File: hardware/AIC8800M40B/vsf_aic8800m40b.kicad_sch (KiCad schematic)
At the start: 86 parts, among them J1 USB_A, J2 USB_C_Receptacle_USB2.0, J3 USB_C_Receptacle_USB2.0, J4 Micro_SD_Card_Det1, J6 Conn_Coaxial, J7 Conn_Coaxial, Q1 S9013, SW1 SW_Push, SW2 SW_Push, SW3 SW_Push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

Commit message: [hardware/aic8800m40b] update
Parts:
- removed D2: 1N5819, vllogic:D_SOD-323_BAT60, symbol Device:D_Schottky
- added C8: 22pF, Capacitor_SMD:C_0805_2012Metric, symbol Device:C
- C16: value 1pF -> 2pF
- C17, C20: value NC -> 0.5pF
- C18: value 0.5pF -> NC
- C22: value NC -> 1.5pF
- J4: footprint (none) -> VSF:MicroSD_Tiny
- J6, J7: footprint (none) -> Connector_Coaxial:U.FL_Molex_MCRF_73412-0110_Vertical
- L3: value 1.2nH -> 1.4nH
- R1: value 1.5nH -> 2nH
- R10: value 80.6k,1% -> 22K,1%
- R14: value 422k,1% -> 100K,1%
- R3: value 1.5nH -> 2pF
- R4: value 1.5nH -> 1.1nH
- U5, U6: footprint (none) -> Filter:Filter_Mini-Circuits_FV1206-1
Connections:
- net LCD_BACKLIGHT is gone; now on net GPIOB4: R13.1
- net USB_D+ is gone; now on net USB_DP: J1.3 (D+), R9.1
- net USB_D- is gone; now on net USB_DM: J1.2 (D-), R8.1
- net GPIOB2: now also J4.9 (DET)
- net PWR_3V3: now also C8.1, L4.2, C8.2
- net at C22.2, R4.1: now also U6.1 (TR_2); no longer U5.1 (TR_2)
- net at R10.2, R14.1, U4.5 (FB): now also C8.1
- net at J7.1 (In): now also U5.5 (RFIN); no longer U6.6 (RFIN)
- net at J6.1 (In): now also U6.5 (RFIN); no longer U5.6 (RFIN)
- net at C18.2, R2.2: now also U5.3 (TR_5); no longer U6.3 (TR_5)
- net at C20.1, R3.1: now also U6.3 (TR_5); no longer U5.3 (TR_5)
- net at C16.1, R1.2: now also U5.1 (TR_2); no longer U6.1 (TR_2)
- net D+: no longer names the net of J2.A6 (D+), J2.B6 (D+), R9.2
- net D-: no longer names the net of J2.A7 (D-), J2.B7 (D-), R8.2
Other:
- moved on the sheet: J5, Q1, R13

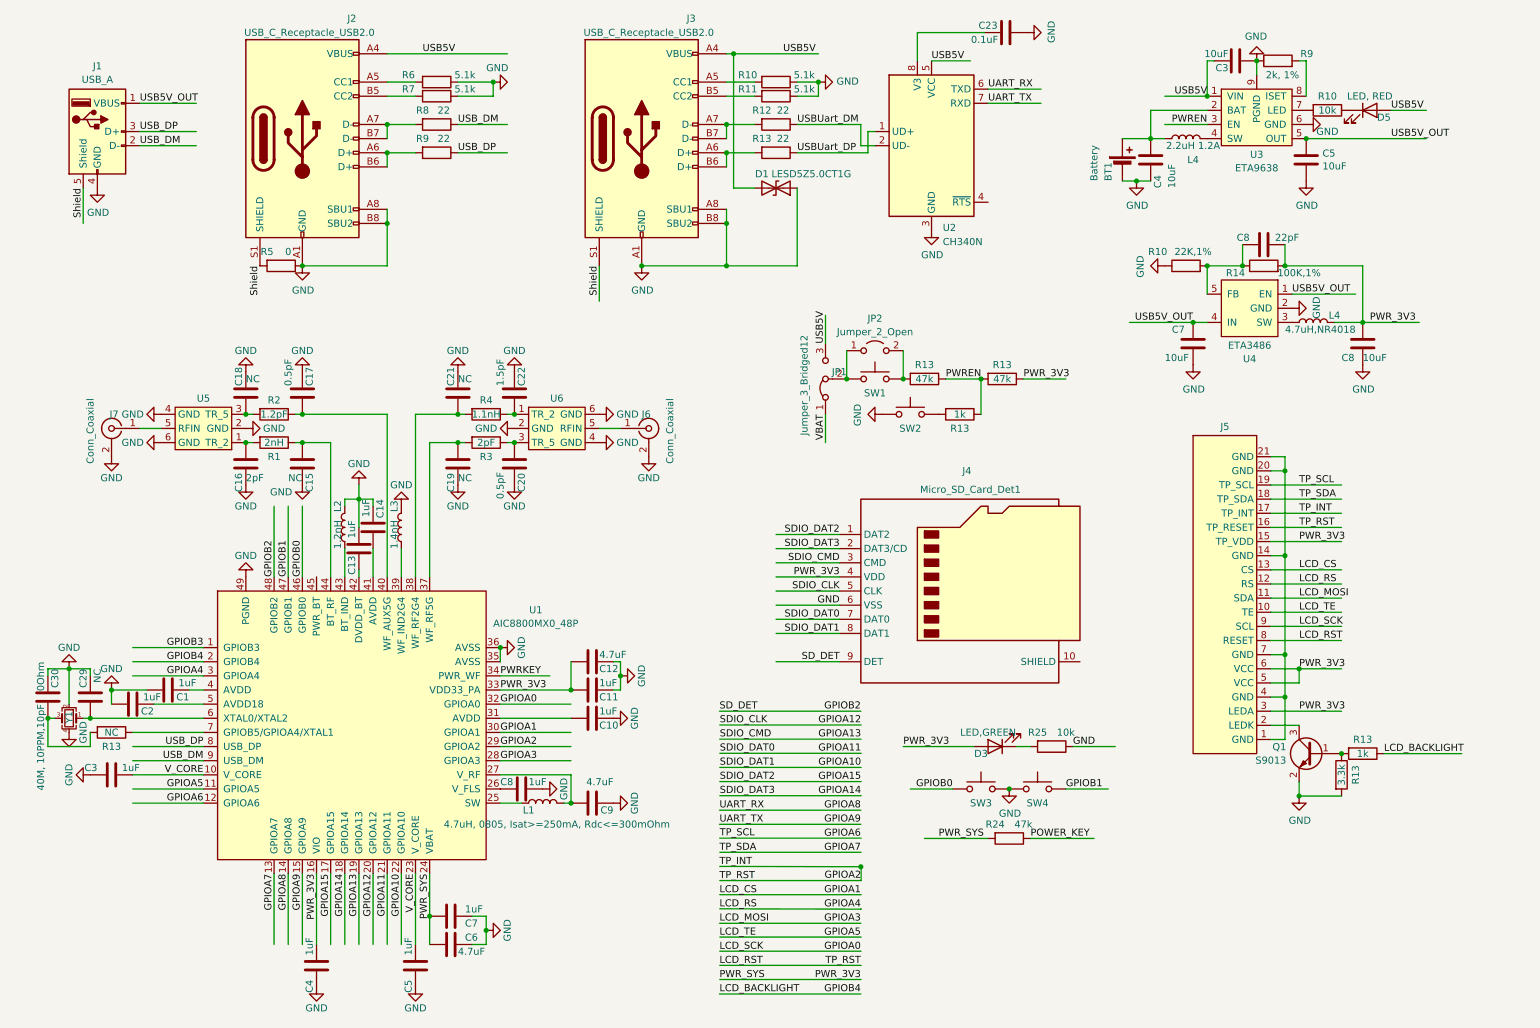
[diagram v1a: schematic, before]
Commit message: [hardware/auc8800m40b] prepare layout
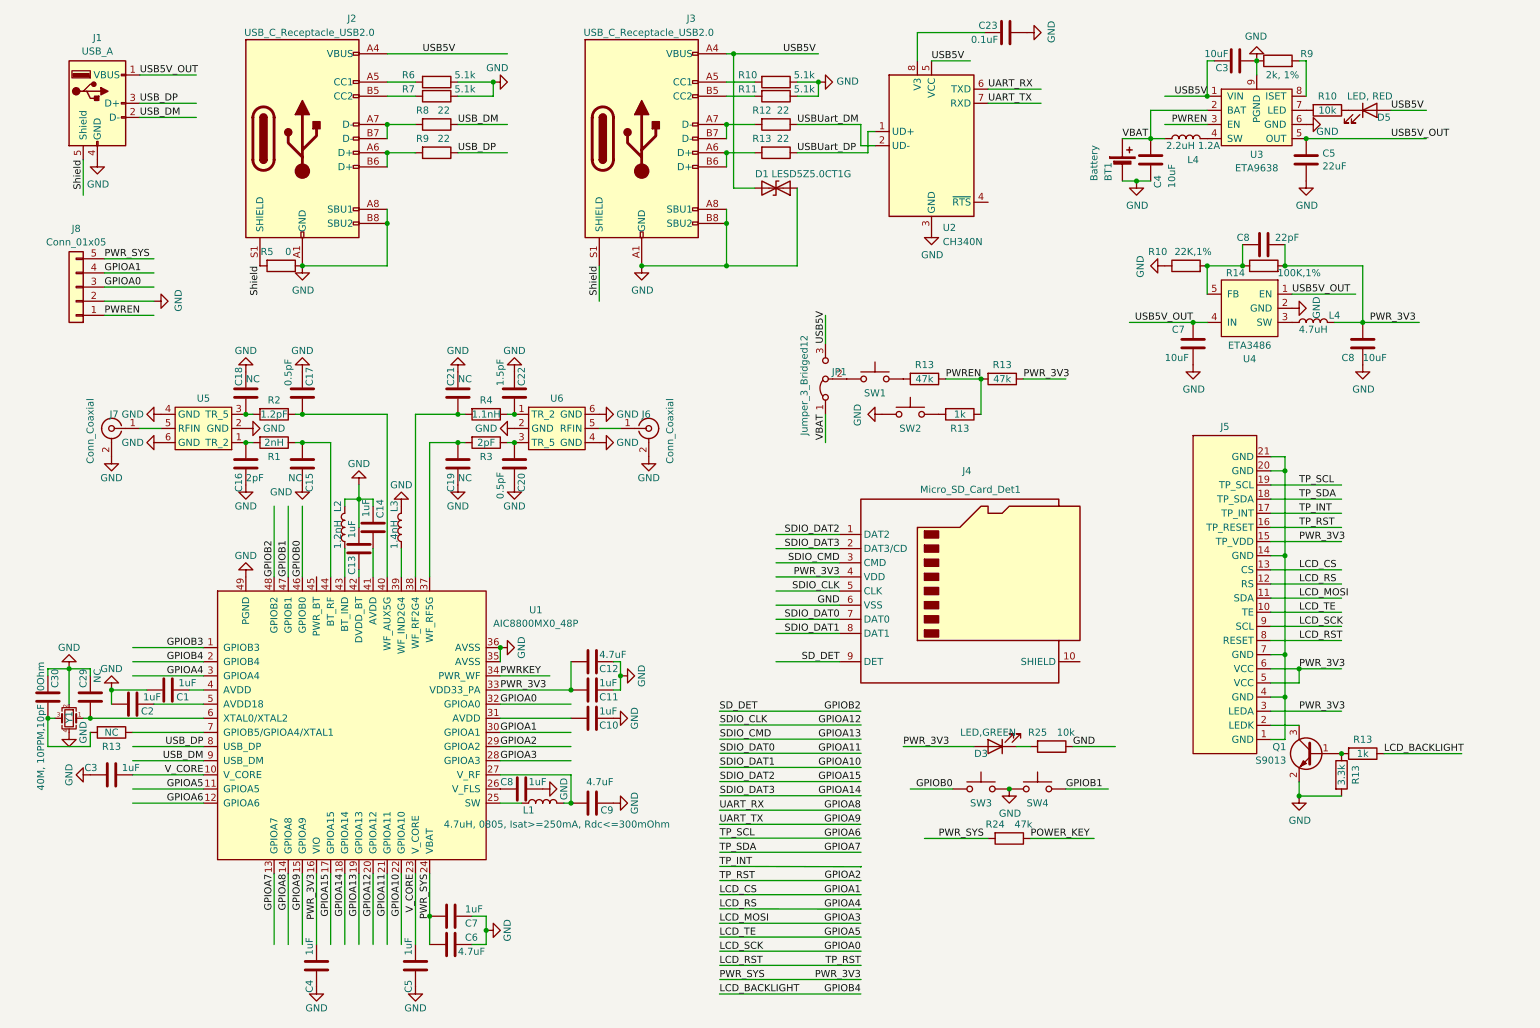
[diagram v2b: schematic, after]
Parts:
- removed JP2: Jumper_2_Open, Jumper:SolderJumper-2_P1.3mm_Open_RoundedPad1.0x1.5mm, symbol Jumper:Jumper_2_Open
- added J8: Conn_01x05, Connector_Harwin:Harwin_M20-89005xx_1x05_P2.54mm_Horizontal, symbol Connector_Generic:Conn_01x05
- C5: value 10uF -> 22uF
- C8: footprint Capacitor_SMD:C_0805_2012Metric -> Capacitor_SMD:C_0402_1005Metric
- L4: value 4.7uH,NR4018 -> 4.7uH; footprint vllogic:L_NR4018 -> Inductor_SMD:L_2010_5025Metric
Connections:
- net GND: now also J8.2 (Pin_2)
- net GPIOA0: now also J8.3 (Pin_3)
- net GPIOA1: now also J8.4 (Pin_4)
- net PWREN: now also J8.1 (Pin_1)
- net PWR_SYS: now also J8.5 (Pin_5)
- net VBAT: now also BT1.1 (+), C4.1, L4.1, U3.2 (BAT)
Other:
- moved on the sheet: J1

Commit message: [hardware/AIC8800M40B] update layout
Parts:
- L2, L3: footprint Inductor_SMD:L_0603_1608Metric -> Inductor_SMD:L_0402_1005Metric
- U1: footprint Package_DFN_QFN:QFN-48-1EP_5x5mm_P0.35mm_EP3.7x3.7mm_ThermalVias -> VSF:QFN-48.10.14.10.14-1EP_5x5mm_P0.35mm_EP3.7x3.7mm_ThermalVias
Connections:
- net POWER_KEY is gone; now on net PWRKEY: R24.1
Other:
- moved on the sheet: C1, C10, C11, C12, C13, C14, C15, C16, C17, C18, C19, C2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

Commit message: [hardware/AIC8800M40B] update
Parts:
- U5, U6: footprint Filter:Filter_Mini-Circuits_FV1206-1 -> VSF:Filter_SLFD18-5R950G-07T
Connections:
- net LCD_CS is gone; now on net GPIOA1: J5.13 (CS)
- net LCD_RS is gone; now on net GPIOA4: J5.12 (RS)
- net LCD_RST is gone; now on net GPIOA2: J5.8 (RESET)
- net LCD_SCK is gone; now on net GPIOA0: J5.9 (SCL)
- net LCD_TE is gone; now on net GPIOA5: J5.10 (TE)
- net PWR_SYS is gone; now on net PWR_3V3: C6.1, C7.1, J8.5 (Pin_5), R24.2, U1.24 (VBAT)
- net TP_INT is gone; now on net GPIOB3: J5.17 (TP_INT)
- net TP_RST is gone; now on net GPIOA2: J5.16 (TP_RESET)
- net TP_SCL is gone; now on net GPIOA6: J5.19 (TP_SCL)
- net TP_SDA is gone; now on net GPIOA7: J5.18 (TP_SDA)
- net GND: now also J5.1 (GND), J5.14 (GND), J5.20 (GND), J5.21 (GND), J5.4 (GND), J5.7 (GND)
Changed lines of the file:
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@@
   (junction (at 26.67 143.51) (diameter 0) (color 0 0 0 0)
   )
+  (junction (at 241.3 93.98) (diameter 0) (color 0 0 0 0)
+  )
   (junction (at 80.01 52.07) (diameter 0) (color 0 0 0 0)
   )
@@
     (stroke (width 0) (type default))
   )
-  (wire (pts (xy 139.7515 182.8189) (xy 165.1515 182.8189))
-    (stroke (width 0) (type default))
-  )
   (wire (pts (xy 36.83 138.43) (xy 30.48 138.43))
     (stroke (width 0) (type default))
@@
     (stroke (width 0) (type default))
   )
-  (wire (pts (xy 165.1 167.64) (xy 165.1515 167.5789))
-    (stroke (width 0) (type default))
-  )
   (wire (pts (xy 74.93 102.87) (xy 74.93 101.6))
     (stroke (width 0) (type default))
@@
     (stroke (width 0) (type default))
   )
-  (wire (pts (xy 139.7515 167.5789) (xy 165.1 167.64))
-    (stroke (width 0) (type default))
-  )
   (wire (pts (xy 85.09 26.67) (xy 80.01 26.67))
     (stroke (width 0) (type default))
@@
     (stroke (width 0) (type default))
   )
+  (wire (pts (xy 139.7 185.42) (xy 165.1 185.42))
+    (stroke (width 0) (type default))
+  )
   (wire (pts (xy 255.27 59.69) (xy 255.27 69.85))
     (stroke (width 0) (type default))
@@
     (stroke (width 0) (type default))
   )
+  (wire (pts (xy 139.7 175.26) (xy 165.1 175.26))
+    (stroke (width 0) (type default))
+  )
   (wire (pts (xy 57.15 168.91) (xy 57.15 181.61))
     (stroke (width 0) (type default))
@@
     (stroke (width 0) (type default))
   )
-  (wire (pts (xy 139.7515 185.3589) (xy 165.1515 185.3589))
-    (stroke (width 0) (type default))
-  )
   (wire (pts (xy 139.7 157.48) (xy 165.1 157.48))
     (stroke (width 0) (type default))
@@
     (stroke (width 0) (type default))
   )
-  (wire (pts (xy 165.1 175.26) (xy 165.1515 175.1989))
-    (stroke (width 0) (type default))
-  )
   (wire (pts (xy 62.23 168.91) (xy 62.23 181.61))
     (stroke (width 0) (type default))
@@
     (stroke (width 0) (type default))
   )
+  (wire (pts (xy 139.7 167.64) (xy 165.1 167.64))
+    (stroke (width 0) (type default))
+  )
   (wire (pts (xy 157.48 29.21) (xy 157.48 26.67))
     (stroke (width 0) (type default))
@@
     (stroke (width 0) (type default))
   )
+  (wire (pts (xy 139.7 180.34) (xy 165.1 180.34))
+    (stroke (width 0) (type default))
+  )
   (wire (pts (xy 172.72 146.05) (xy 185.42 146.05))
     (stroke (width 0) (type default))
@@
     (stroke (width 0) (type default))
   )
+  (wire (pts (xy 139.7 172.72) (xy 165.1 172.72))
+    (stroke (width 0) (type default))
+  )
   (wire (pts (xy 92.71 26.67) (xy 99.06 26.67))
     (stroke (width 0) (type default))
@@
     (stroke (width 0) (type default))
   )
-  (wire (pts (xy 139.7515 162.4989) (xy 165.1515 162.4989))
-    (stroke (width 0) (type default))
-  )
   (wire (pts (xy 139.7515 149.7989) (xy 165.1515 149.7989))
     (stroke (width 0) (type default))
@@
     (stroke (width 0) (type default))
   )
-  (wire (pts (xy 139.7515 187.8989) (xy 165.1515 187.8989))
+  (wire (pts (xy 34.29 130.81) (xy 46.99 130.81))
     (stroke (width 0) (type default))
   )
-  (wire (pts (xy 34.29 130.81) (xy 46.99 130.81))
+  (wire (pts (xy 139.7 165.1) (xy 165.1 165.1))
     (stroke (width 0) (type default))
   )
@@
     (stroke (width 0) (type default))
   )
+  (wire (pts (xy 139.7 182.88) (xy 165.1 182.88))
+    (stroke (width 0) (type default))
+  )
   (wire (pts (xy 139.7515 142.1789) (xy 165.1515 142.1789))
     (stroke (width 0) (type default))
@@
     (stroke (width 0) (type default))
   )
-  (wire (pts (xy 139.7515 165.0389) (xy 165.1515 165.0389))
-    (stroke (width 0) (type default))
-  )
   (wire (pts (xy 74.93 101.6) (xy 72.39 101.6))
     (stroke (width 0) (type default))
@@
     (stroke (width 0) (type default))
   )
-  (wire (pts (xy 165.1515 167.64) (xy 165.1 167.64))
-    (stroke (width 0) (type default))
-  )
   (wire (pts (xy 59.69 168.91) (xy 59.69 181.61))
     (stroke (width 0) (type default))
@@
     (stroke (width 0) (type default))
   )
-  (wire (pts (xy 139.7515 170.1189) (xy 165.1515 170.1189))
-    (stroke (width 0) (type default))
-  )
   (wire (pts (xy 100.33 130.81) (xy 109.22 130.81))
     (stroke (width 0) (type default))
   )
-  (wire (pts (xy 139.7515 172.6589) (xy 165.1515 172.6589))
-    (stroke (width 0) (type default))
-  )
   (wire (pts (xy 80.01 21.59) (xy 101.6 21.59))
     (stroke (width 0) (type default))
@@
     (stroke (width 0) (type default))
   )
-  (wire (pts (xy 139.7515 180.2789) (xy 165.1515 180.2789))
+  (wire (pts (xy 139.7 162.56) (xy 165.1 162.56))
     (stroke (width 0) (type default))
   )
@@
     (stroke (width 0) (type default))
   )
+  (wire (pts (xy 139.7 187.96) (xy 165.1 187.96))
+    (stroke (width 0) (type default))
+  )
   (wire (pts (xy 238.76 139.7) (xy 251.46 139.7))
     (stroke (width 0) (type default))
@@
     (stroke (width 0) (type default))
   )
+  (wire (pts (xy 139.7 170.18) (xy 165.1 170.18))
+    (stroke (width 0) (type default))
+  )
   (wire (pts (xy 140.97 21.59) (xy 142.24 21.59))
     (stroke (width 0) (type default))
@@
     (stroke (width 0) (type default))
   )
-  (wire (pts (xy 139.7515 175.1989) (xy 165.1 175.26))
-    (stroke (width 0) (type default))
-  )
   (wire (pts (xy 67.31 115.57) (xy 67.31 91.44))
     (stroke (width 0) (type default))
@@
     (effects (font (size 1.27 1.27)) (justify left bottom))
   )
-  (label "TP_SCL" (at 139.7515 162.4989 0) (fields_autoplaced)
+  (label "TP_SCL" (at 139.7 162.56 0) (fields_autoplaced)
     (effects (font (size 1.27 1.27)) (justify left bottom))
   )
@@
     (effects (font (size 1.27 1.27)) (justify right bottom))
   )
-  (label "TP_SDA" (at 139.7 165.1 0) (fields_autoplaced)
-    (effects (font (size 1.27 1.27)) (justify left bottom))
-  )
   (label "LCD_BACKLIGHT" (at 139.7 190.5 0) (fields_autoplaced)
     (effects (font (size 1.27 1.27)) (justify left bottom))
@@
     (effects (font (size 1.27 1.27)) (justify right bottom))
   )
+  (label "TP_SDA" (at 139.7 165.1 0) (fields_autoplaced)
+    (effects (font (size 1.27 1.27)) (justify left bottom))
+  )
   (label "SDIO_CMD" (at 139.7515 144.7189 0) (fields_autoplaced)
     (effects (font (size 1.27 1.27)) (justify left bottom))
@@
     (effects (font (size 1.27 1.27)) (justify right bottom))
   )
+  (label "GPIOB3" (at 165.1 167.64 180) (fields_autoplaced)
+    (effects (font (size 1.27 1.27)) (justify right bottom))
+  )
   (label "GPIOA7" (at 165.1 165.1 180) (fields_autoplaced)
     (effects (font (size 1.27 1.27)) (justify right bottom))
@@
     (effects (font (size 1.27 1.27)) (justify left bottom))
   )
-  (label "GPIOA2" (at 165.1515 170.1189 180) (fields_autoplaced)
+  (label "GPIOA2" (at 165.1 170.18 180) (fields_autoplaced)
     (effects (font (size 1.27 1.27)) (justify right bottom))
   )
@@
     )
   )
+  (symbol (lib_id "power:GND") (at 241.3 93.98 90) (unit 1)
+    (in_bom yes) (on_board yes) (dnp no)
+    (property "Reference" "#PWR051" (at 247.65 93.98 0)
+      (effects (font (size 1.27 1.27)) hide)
+    )
+    (property "Value" "GND" (at 245.6942 93.853 0)
+      (effects (font (size 1.27 1.27)))
+    )
+    (property "Footprint" "" (at 241.3 93.98 0)
+      (effects (font (size 1.27 1.27)) hide)
+    )
+    (property "Datasheet" "" (at 241.3 93.98 0)
+      (effects (font (size 1.27 1.27)) hide)
+    )
+    (pin "1")
+    (instances
+      (project "vsf_aic8800m40b"
+        (path "/7ff897c7-5676-47e3-800e-188ea4d80e23"
+          (reference "#PWR051") (unit 1)
+        )
+      )
+      (project "MCULinux"
+        (path "/b0717bb8-5e5d-44de-b48f-ff278896fb50"
+          (reference "#PWR035") (unit 1)
+        )
+      )
+      (project "uikit"
+        (path "/ec8c2704-3ff6-4923-b467-189ddf2567d5"
+          (reference "#PWR011") (unit 1)
+        )
+      )
+    )
+  )
   (symbol (lib_id "Device:R") (at 251.46 151.13 0) (unit 1)
     (in_bom yes) (on_board yes) (dnp no)
@@
       (effects (font (size 1.27 1.27)))
     )
-    (property "Footprint" "Filter:Filter_Mini-Circuits_FV1206-1" (at 107.95 81.28 0)
+    (property "Footprint" "VSF:Filter_SLFD18-5R950G-07T" (at 107.95 81.28 0)
       (effects (font (size 1.27 1.27)) hide)
     )
@@
       (effects (font (size 1.27 1.27)))
     )
-    (property "Footprint" "Filter:Filter_Mini-Circuits_FV1206-1" (at 44.45 96.52 0)
+    (property "Footprint" "VSF:Filter_SLFD18-5R950G-07T" (at 44.45 96.52 0)
       (effects (font (size 1.27 1.27)) hide)
     )
